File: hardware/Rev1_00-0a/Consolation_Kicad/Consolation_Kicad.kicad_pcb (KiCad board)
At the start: 2 copper layers, 137.5 x 76.6 mm, 392 parts, among them J10 61300311121, J11 5051102291, J12 RPI_CMx_B, J13 5051102291, J14 61300311121, J15 61300311121, J17 61300311121, J18 61300411121, J19 RPI_CMx_A, J2 SJ-3524-SMT-TR, J3 62684-402100ALF, J4 12401598E4#2A, J5 S2B-PH-K-S, J6 2086581001, J7 2998TR, J8 DM3AT-SF-PEJM5, Q1 SSM3K56FS,LF, Q10 SSM3K56FS,LF, Q11 SSM3K56FS,LF, Q14 SSM3K56FS,LF, Q18 SSM3K56FS,LF, Q19 SSM3K56FS,LF, Q2 SSM3K56FS,LF, Q20 SSM3K56FS,LF, Q21 SSM3K56FS,LF, Q22 SSM3K56FS,LF, Q23 SSM3K56FS,LF, Q24 SSM3K56FS,LF, Q25 SSM3K56FS,LF, Q26 SSM3K56FS,LF, Q27 SSM3K56FS,LF, Q28 SSM3K56FS,LF, Q3 SSM3K56FS,LF, Q7 SSM3K56FS,LF, Q8 SSM3K56FS,LF, Q9 SSM3K56FS,LF, U1 BQ25640VDLR, U10 TPS62826DMQR, U11 AP22913W6-7, U15 SN65DSI84ZXHR, U18 AP22913W6-7, U19 SN74LVC1G125DBVR, U2 RP2350A, U21 MCP7940NT-I/MS, U26 TPS61169DCKR, U30 STM6710DWB6F, U31 SN74LVC1G125DBVR, U32 SN74HCS365QPWRQ1, U4 ECS-2016MVQ-120-BP-TR, U5 NAU88C22YG, U6 AP22913W6-7, U7 TPS79901DRVR, U8 GD25Q32CWIGR, U9 TPS61230ARNSR, Y1 12MHz 10pF, Y2 32.768kHz

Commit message: Component preliminary placement
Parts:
- removed R136: 22R, footprint:RES_0402
- added R212: 10K, footprint:RES_0402, F.Cu at (151.1, 155.3)
- moved C123 420.3 mm to (35.9, 25.2)
- moved R121 420.3 mm to (24.6, 24.6)
- moved R124 420.3 mm to (24.6, 26.6)
- moved R176 420.3 mm to (24.6, 28.8)
- moved R180 420.3 mm to (24.6, 30.9)
- moved R40 420.3 mm to (24.6, 20.4)
- moved R41 420.3 mm to (24.6, 22.4)
- moved C122 420.3 mm to (35.9, 23.1)
- moved D13 420.3 mm to (36.2, 18.4)
- moved D14 420.3 mm to (36.2, 20.8)
- moved D19 420.3 mm to (20.2, 34.6)
- moved Q14 420.3 mm to (37.1, 30.6)
- moved HOLE7 377.0 mm to (58.9, 53.4)
- moved J5 368.3 mm to (51.9, 109.4), turned to -90 degrees
- moved HOLE6 364.5 mm to (58.9, 123.4)
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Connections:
- J19 pad 24: /CM5_CONN_A/GPIO19 -> /CM5_CONN_A/GPIO26
- J19 pad 45: /CM5_CONN_A/GPIO24 -> unconnected-(J19-GPIO24-Pad45)
- R171 pad 1: /CM5_CONN_A/GPIO19 -> /CM5_CONN_A/GPIO26
- R209 pad 2: /~{TFT_RST} -> /TFT CONN/TFT_3V3
- R211 pad 2: /TFT_PWR_EN -> /~{TFT_RST}
- R271 pad 2: 3V3 -> 5V0
- U11 pad 3: /TFT_PWR_EN -> /~{TFT_RST}
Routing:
- added copper zone on In1.Cu, net GND
- added copper zone on In4.Cu, net GND
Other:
- copper layers 2 -> 6

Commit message: Preliminary placement of Consolation continues
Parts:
- removed C115, C116: 0.1u, footprint:CAP_NONPOL_0402
- removed D44, D45: D1213A-02SOL-7, footprint:SOT-23-3
- removed R13, R14, R15, R16, R17: 10K, footprint:RES_ARRAY_4_1206
- added D1: ESD7351HT1G, footprint:SOD-323, F.Cu at (76.0, 52.4)
- added D20: ESD7351HT1G, footprint:SOD-323, F.Cu at (56.2, 147.5)
- added D23: ESD7351HT1G, footprint:SOD-323, F.Cu at (56.2, 150.3)
- added D24: ESD7351HT1G, footprint:SOD-323, F.Cu at (56.2, 153.0)
- added D25: ESD7351HT1G, footprint:SOD-323, F.Cu at (56.2, 155.8)
- added D26: ESD7016MUTAG, footprint:UDFN8, F.Cu at (108.8, 114.5)
- added R181: 10K, footprint:RES_0402, F.Cu at (66.1, 59.6)
- added R185: 10K, footprint:RES_0402, F.Cu at (66.1, 61.7)
- added R186: 10K, footprint:RES_0402, F.Cu at (66.1, 63.8)
- added R187: 10K, footprint:RES_0402, F.Cu at (66.1, 65.9)
- added R188: 10K, footprint:RES_0402, F.Cu at (66.1, 68.0)
- added R189: 10K, footprint:RES_0402, F.Cu at (69.1, 59.6)
- added R190: 10K, footprint:RES_0402, F.Cu at (69.1, 61.7)
- added R191: 10K, footprint:RES_0402, F.Cu at (69.1, 63.8)
- added R192: 10K, footprint:RES_0402, F.Cu at (69.1, 65.9)
- added R193: 10K, footprint:RES_0402, F.Cu at (69.1, 68.0)
- added R194: 10K, footprint:RES_0402, F.Cu at (72.1, 59.6)
- added R195: 10K, footprint:RES_0402, F.Cu at (72.1, 61.7)
- added R196: 10K, footprint:RES_0402, F.Cu at (72.1, 63.8)
- added R197: 10K, footprint:RES_0402, F.Cu at (72.1, 65.9)
- added R198: 10K, footprint:RES_0402, F.Cu at (72.1, 68.0)
- added R199: 10K, footprint:RES_0402, F.Cu at (75.1, 59.6)
- added R200: 10K, footprint:RES_0402, F.Cu at (75.1, 61.7)
- added R201: 10K, footprint:RES_0402, F.Cu at (75.1, 63.8)
- added R202: 10K, footprint:RES_0402, F.Cu at (75.1, 65.9)
- added R203: 10K, footprint:RES_0402, F.Cu at (75.1, 68.0)
- D19: value D1213A-02SOL-7 -> ESD7351HT1G; footprint footprint:SOT-23-3 -> footprint:SOD-323
- moved D19 122.8 mm to (141.7, 52.4), turned to -90 degrees
- moved R121 118.7 mm to (140.2, 51.7), turned to 90 degrees
- moved R120 64.3 mm to (106.5, 83.0)
- moved R141 63.1 mm to (131.6, 81.1), turned to 180 degrees
- moved R140 61.8 mm to (131.6, 77.7)
- moved R171 60.8 mm to (131.6, 82.2), turned to 180 degrees
- moved R127 60.2 mm to (131.6, 78.8), turned to 180 degrees
- moved R144 59.9 mm to (131.6, 80.0), turned to 180 degrees
- moved R115 59.9 mm to (140.4, 81.5)
- moved R125 59.3 mm to (140.4, 74.5)
- moved R124 58.6 mm to (77.6, 51.7), turned to 90 degrees
- moved R117 58.0 mm to (140.4, 83.8)
- moved R161 57.3 mm to (131.6, 76.5), turned to 180 degrees
- moved R116 56.6 mm to (140.4, 80.3), turned to 180 degrees
- moved R83 55.6 mm to (131.6, 74.5), turned to 180 degrees
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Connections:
- C122 pad 2: Net-(C122-Pad2) -> Net-(D19-K)
- D19 pad 1: /CM5_CONN_A/~{VOL_UP} -> Net-(D19-K)
- D19 pad 2: /CM5_CONN_A/~{VOL_DOWN} -> GND
- D5 pad 1: /CONTROLLER/L_THUMBST_SW -> /CONTROLLER/L_THUMBST_X
- D5 pad 2: /CONTROLLER/L_DPAD_UP -> /CONTROLLER/L_THUMBST_Y
- D5 pad 4: /CONTROLLER/L_DPAD_DOWN -> /CONTROLLER/L_THUMBST_SW
- D5 pad 5: /CONTROLLER/L_DPAD_LEFT -> /CONTROLLER/L_DPAD_UP
- D5 pad 7: /CONTROLLER/L_DPAD_RIGHT -> /CONTROLLER/L_DPAD_DOWN
- D5 pad 8: /CONTROLLER/L_START -> unconnected-(D5-I/O6-Pad8)
- D6 pad 1: /CONTROLLER/R_THUMBST_SW -> /CONTROLLER/R_THUMBST_X
- D6 pad 2: /CONTROLLER/R_BTN_A -> /CONTROLLER/R_THUMBST_Y
- D6 pad 4: /CONTROLLER/R_BTN_B -> /CONTROLLER/R_THUMBST_SW
- D6 pad 5: /CONTROLLER/R_BTN_X -> /CONTROLLER/R_BTN_A
- D6 pad 7: /CONTROLLER/R_BTN_Y -> /CONTROLLER/R_BTN_B
- D6 pad 8: /CONTROLLER/R_SELECT -> unconnected-(D6-I/O6-Pad8)
- D8 pad 1: /CONTROLLER/L_L1_TRIG -> /CONTROLLER/L_DPAD_LEFT
- D8 pad 2: /CONTROLLER/L_L2_TRIG -> /CONTROLLER/L_DPAD_RIGHT
- D8 pad 4: /CONTROLLER/L_HOME -> /CONTROLLER/L_START
- D8 pad 5: unconnected-(D8-I/O4-Pad5) -> /CONTROLLER/L_L1_TRIG
- D8 pad 7: unconnected-(D8-I/O5-Pad7) -> /CONTROLLER/L_L2_TRIG
- D8 pad 8: unconnected-(D8-I/O6-Pad8) -> /CONTROLLER/L_HOME
- D9 pad 1: /CONTROLLER/R_L1_TRIG -> /CONTROLLER/R_BTN_X
- D9 pad 2: /CONTROLLER/R_L2_TRIG -> /CONTROLLER/R_BTN_Y
- D9 pad 4: /CONTROLLER/R_EXTRA -> /CONTROLLER/R_SELECT
- D9 pad 5: unconnected-(D9-I/O4-Pad5) -> /CONTROLLER/R_L1_TRIG
- D9 pad 7: unconnected-(D9-I/O5-Pad7) -> /CONTROLLER/R_L2_TRIG
- D9 pad 8: unconnected-(D9-I/O6-Pad8) -> /CONTROLLER/R_EXTRA
- R121 pad 2: Net-(C122-Pad2) -> Net-(D19-K)
- R127 pad 1: /CM5_CONN_A/I2C3.I2C_SCL -> /I2C2.I2C_SCL
- R176 pad 1: Net-(C122-Pad2) -> Net-(D19-K)
- R83 pad 1: /CM5_CONN_A/I2C3.I2C_SDA -> /I2C2.I2C_SDA
- S2 pad 2: Net-(C122-Pad2) -> Net-(D19-K)
- U21 pad 5: /CM5_CONN_A/I2C3.I2C_SDA -> /I2C2.I2C_SDA
- U21 pad 6: /CM5_CONN_A/I2C3.I2C_SCL -> /I2C2.I2C_SCL
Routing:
- net /CM5_CONN_A/GPIO12: track 0.00 -> 2.66 mm
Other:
- board text added: "Controller - L"
- board text added: "Controller - R"

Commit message: Work on preliminary placement + RP2350A fanout
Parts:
- removed C128, C130: 1u, footprint:CAP_NONPOL_0805
- removed C129, C131, C151: 0.1u, footprint:CAP_NONPOL_0402
- removed C13, C14: 10u, footprint:CAP_NONPOL_1210
- removed R11: 0R, footprint:RES_0603
- removed R160: 10K, footprint:RES_0402
- removed R4: 0R, footprint:RES_1206
- added C45: 4.7u, footprint:CAP_NONPOL_0805, F.Cu at (87.0, 58.6)
- added C46: 4.7u, footprint:CAP_NONPOL_0805, F.Cu at (87.0, 56.6)
- added R13: 0R, footprint:RES_1206, F.Cu at (43.1, 86.6)
- added R14: 0R, footprint:RES_1206, F.Cu at (20.8, 105.0)
- added R204: 0R, footprint:RES_0402, F.Cu at (84.7, 71.6)
- moved R182 168.1 mm to (22.6, 123.0)
- moved R168 167.9 mm to (25.1, 124.4)
- moved R43 166.7 mm to (27.6, 123.9)
- moved C155 75.8 mm to (144.3, 85.7), turned to 90 degrees
- moved C16 54.0 mm to (85.5, 73.3), turned to 180 degrees
- moved D11 53.1 mm to (21.7, 66.2)
- moved S1 52.1 mm to (55.1, 59.1), turned to -90 degrees
- moved C17 51.2 mm to (83.3, 73.3)
- moved C140 51.1 mm to (90.0, 71.7), turned to 90 degrees
- moved R280 51.0 mm to (87.8, 73.9), turned to 90 degrees
- moved C120 50.1 mm to (17.3, 69.6)
- moved C147 48.3 mm to (91.7, 72.2), turned to 90 degrees
- moved C134 47.3 mm to (91.0, 64.8), turned to 180 degrees
- moved R37 45.8 mm to (43.8, 71.6), turned to -90 degrees
- moved C27 45.8 mm to (44.7, 74.4)
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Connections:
- net /CM5_CONN_B/RP2350_USB_VBUS renamed /CM5_CONN_B/RP2350_VBUS
- net Net-(U2B-USB_DN) renamed /CONTROLLER/USB_N
- net Net-(U2B-USB_DP) renamed /CONTROLLER/USB_P
- C103 pad 2: /Power Supply/VSYS -> Net-(U10-VIN)
- C23 pad 2: /Power Supply/VSYS -> Net-(L3-+)
- C24 pad 2: /Power Supply/VSYS -> Net-(L3-+)
- C29 pad 2: /Power Supply/VSYS -> Net-(L3-+)
- C30 pad 2: /Power Supply/VSYS -> Net-(U10-VIN)
- C31 pad 2: /Power Supply/VSYS -> Net-(U10-VIN)
- C32 pad 2: /Power Supply/VSYS -> Net-(U10-VIN)
- C6 pad 2: Net-(L1--) -> /Power Supply/VSYS
- C7 pad 2: Net-(L1--) -> /Power Supply/VSYS
- C91 pad 2: Net-(L1--) -> /Power Supply/VSYS
- C98 pad 2: /Power Supply/VSYS -> Net-(L3-+)
- D26 pad 1: unconnected-(D26-I/O1-Pad1) -> Net-(D26-I/O1)
- D26 pad 7: Net-(D26-I/O5) -> unconnected-(D26-I/O5-Pad7)
- J4 pad A5: Net-(D26-I/O5) -> Net-(D26-I/O1)
- L1 pad 2: Net-(L1--) -> /Power Supply/VSYS
- L3 pad 1: /Power Supply/VSYS -> Net-(L3-+)
- R10 pad 1: /CONTROLLER/CM5_USB3_1.USB_N -> /CM5_CONN_B/USB2_RP2350.USB_N
- R157 pad 1: /CONTROLLER/L_THUMBST_SW -> /CONTROLLER/L_DPAD_LEFT
- R159 pad 1: /CONTROLLER/R_THUMBST_SW -> /CONTROLLER/L_DPAD_RIGHT
- R181 pad 1: /CONTROLLER/L_HOME -> /CONTROLLER/R_THUMBST_X
- R185 pad 1: /CONTROLLER/R_EXTRA -> /CONTROLLER/R_THUMBST_Y
- R186 pad 1: /CONTROLLER/R_BTN_Y -> /CONTROLLER/L_DPAD_DOWN
- R187 pad 1: /CONTROLLER/R_BTN_X -> /CONTROLLER/L_DPAD_UP
- R188 pad 1: /CONTROLLER/R_BTN_B -> /CONTROLLER/L_THUMBST_SW
- R189 pad 1: /CONTROLLER/R_BTN_A -> /CONTROLLER/L_THUMBST_Y
- R190 pad 1: /CONTROLLER/L_START -> /CONTROLLER/R_EXTRA
- R191 pad 1: /CONTROLLER/R_SELECT -> /CONTROLLER/L_THUMBST_X
- R192 pad 1: /CONTROLLER/L_THUMBST_X -> /CONTROLLER/L_START
- R193 pad 1: /CONTROLLER/L_THUMBST_Y -> /CONTROLLER/L_L1_TRIG
- R194 pad 1: /CONTROLLER/R_THUMBST_X -> /CONTROLLER/L_L2_TRIG
- R195 pad 1: /CONTROLLER/R_THUMBST_Y -> /CONTROLLER/L_HOME
- R196 pad 1: /CONTROLLER/L_DPAD_RIGHT -> /CONTROLLER/R_L2_TRIG
- R197 pad 1: /CONTROLLER/L_DPAD_LEFT -> /CONTROLLER/R_L1_TRIG
- R198 pad 1: /CONTROLLER/L_DPAD_DOWN -> /CONTROLLER/R_SELECT
- R199 pad 1: /CONTROLLER/L_DPAD_UP -> /CONTROLLER/R_BTN_Y
- R200 pad 1: /CONTROLLER/R_L2_TRIG -> /CONTROLLER/R_BTN_X
- R201 pad 1: /CONTROLLER/R_L1_TRIG -> /CONTROLLER/R_BTN_B
- R202 pad 1: /CONTROLLER/L_L2_TRIG -> /CONTROLLER/R_BTN_A
- R203 pad 1: /CONTROLLER/L_L1_TRIG -> /CONTROLLER/R_THUMBST_SW
- R37 pad 2: /Power Supply/VSYS -> Net-(L3-+)
- R9 pad 1: /CONTROLLER/CM5_USB3_1.USB_P -> /CM5_CONN_B/USB2_RP2350.USB_P
- U1 pad 1: Net-(D26-I/O5) -> Net-(D26-I/O1)
- U1 pad 13: Net-(L1--) -> /Power Supply/VSYS
- U10 pad 6: /Power Supply/VSYS -> Net-(U10-VIN)
- U2 pad 10: /CONTROLLER/R_EXTRA -> /CONTROLLER/R_THUMBST_Y
- U2 pad 12: /CONTROLLER/L_L1_TRIG -> /CONTROLLER/R_THUMBST_SW
- U2 pad 13: /CONTROLLER/L_L2_TRIG -> /CONTROLLER/R_BTN_A
- U2 pad 14: /CONTROLLER/R_L1_TRIG -> /CONTROLLER/R_BTN_B
- U2 pad 15: /CONTROLLER/R_L2_TRIG -> /CONTROLLER/R_BTN_X
- U2 pad 16: /CONTROLLER/L_DPAD_UP -> /CONTROLLER/R_BTN_Y
- U2 pad 17: /CONTROLLER/L_DPAD_DOWN -> /CONTROLLER/R_SELECT
- U2 pad 18: /CONTROLLER/L_DPAD_LEFT -> /CONTROLLER/R_L1_TRIG
- U2 pad 19: /CONTROLLER/L_DPAD_RIGHT -> /CONTROLLER/R_L2_TRIG
- U2 pad 27: /CONTROLLER/L_START -> /CONTROLLER/R_EXTRA
- U2 pad 28: /CONTROLLER/R_SELECT -> /CONTROLLER/L_THUMBST_X
- U2 pad 31: /CONTROLLER/R_BTN_A -> /CONTROLLER/L_THUMBST_Y
- U2 pad 32: /CONTROLLER/R_BTN_B -> /CONTROLLER/L_THUMBST_SW
- U2 pad 33: /CONTROLLER/R_BTN_X -> /CONTROLLER/L_DPAD_UP
- U2 pad 34: /CONTROLLER/R_BTN_Y -> /CONTROLLER/L_DPAD_DOWN
- U2 pad 35: /CONTROLLER/L_THUMBST_SW -> /CONTROLLER/L_DPAD_LEFT
- U2 pad 37: /CONTROLLER/R_THUMBST_SW -> /CONTROLLER/L_DPAD_RIGHT
- U2 pad 40: /CONTROLLER/L_THUMBST_X -> /CONTROLLER/L_START
- U2 pad 41: /CONTROLLER/L_THUMBST_Y -> /CONTROLLER/L_L1_TRIG
- U2 pad 42: /CONTROLLER/R_THUMBST_X -> /CONTROLLER/L_L2_TRIG
- U2 pad 43: /CONTROLLER/R_THUMBST_Y -> /CONTROLLER/L_HOME
- U2 pad 9: /CONTROLLER/L_HOME -> /CONTROLLER/R_THUMBST_X
- U9 pad 2: /Power Supply/VSYS -> Net-(L3-+)
- U9 pad 4: /Power Supply/VSYS -> Net-(L3-+)
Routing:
- net GND: track 0.00 -> 37.1 mm, vias 0 -> 45
- net 3V3: track 0.00 -> 27.0 mm, vias 0 -> 10
- net /CONTROLLER/1V1_CORE: track 0.00 -> 18.4 mm, vias 0 -> 5
- net /CONTROLLER/R_BTN_Y: track 0.00 -> 11.0 mm
- net /CONTROLLER/R_SELECT: track 0.00 -> 10.7 mm
- net /CONTROLLER/R_L1_TRIG: track 0.00 -> 10.2 mm
- net /CONTROLLER/L_THUMBST_X: track 0.00 -> 9.75 mm
- net /CONTROLLER/L_THUMBST_Y: track 0.00 -> 9.73 mm
- net /CONTROLLER/R_L2_TRIG: track 0.00 -> 9.71 mm
- net /CONTROLLER/R_BTN_X: track 0.00 -> 9.41 mm
- net /CONTROLLER/R_THUMBST_Y: track 0.00 -> 9.26 mm
- net /CONTROLLER/L_THUMBST_SW: track 0.00 -> 9.12 mm
- net /CONTROLLER/L_DPAD_RIGHT: track 0.00 -> 9.11 mm
- net /CONTROLLER/R_EXTRA: track 0.00 -> 8.99 mm
- net /CONTROLLER/R_BTN_B: track 0.00 -> 8.91 mm
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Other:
- outline, holes or cut-outs redrawn
- board text added: "~{RP2350 USB BOOT}"

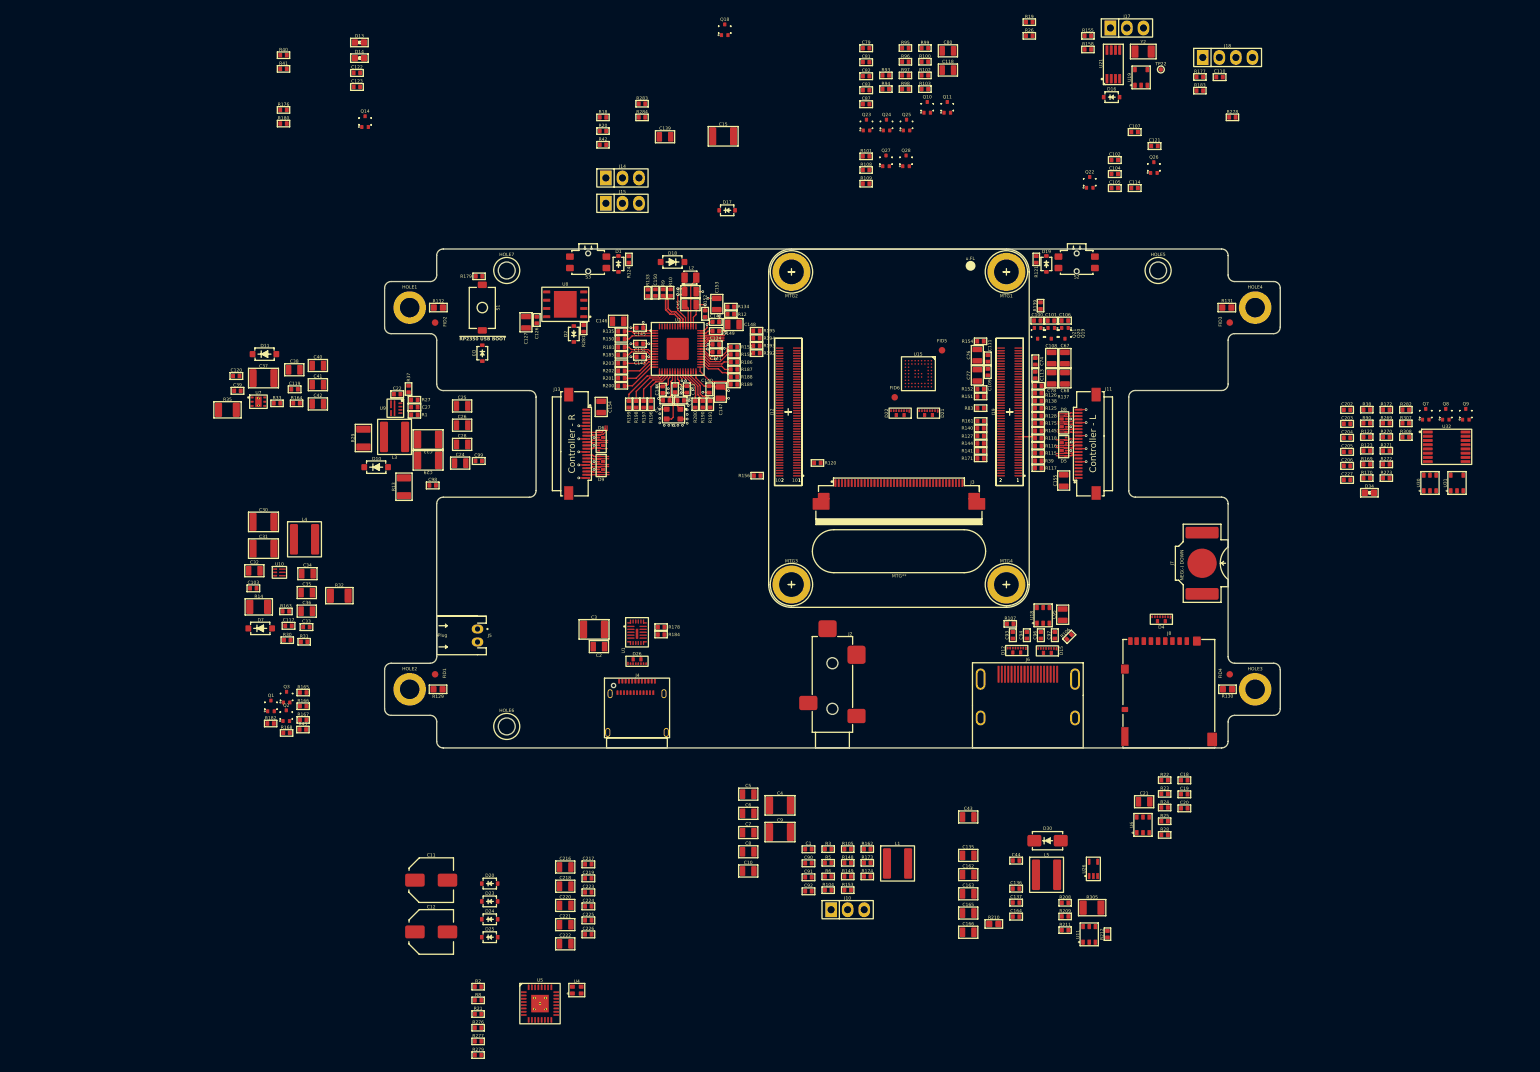
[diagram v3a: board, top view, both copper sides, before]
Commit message: Update ConJoy L2 trigger (2-level trigger instead) Update ConJoy all output files accordingly
Work on Consolation preliminary placement
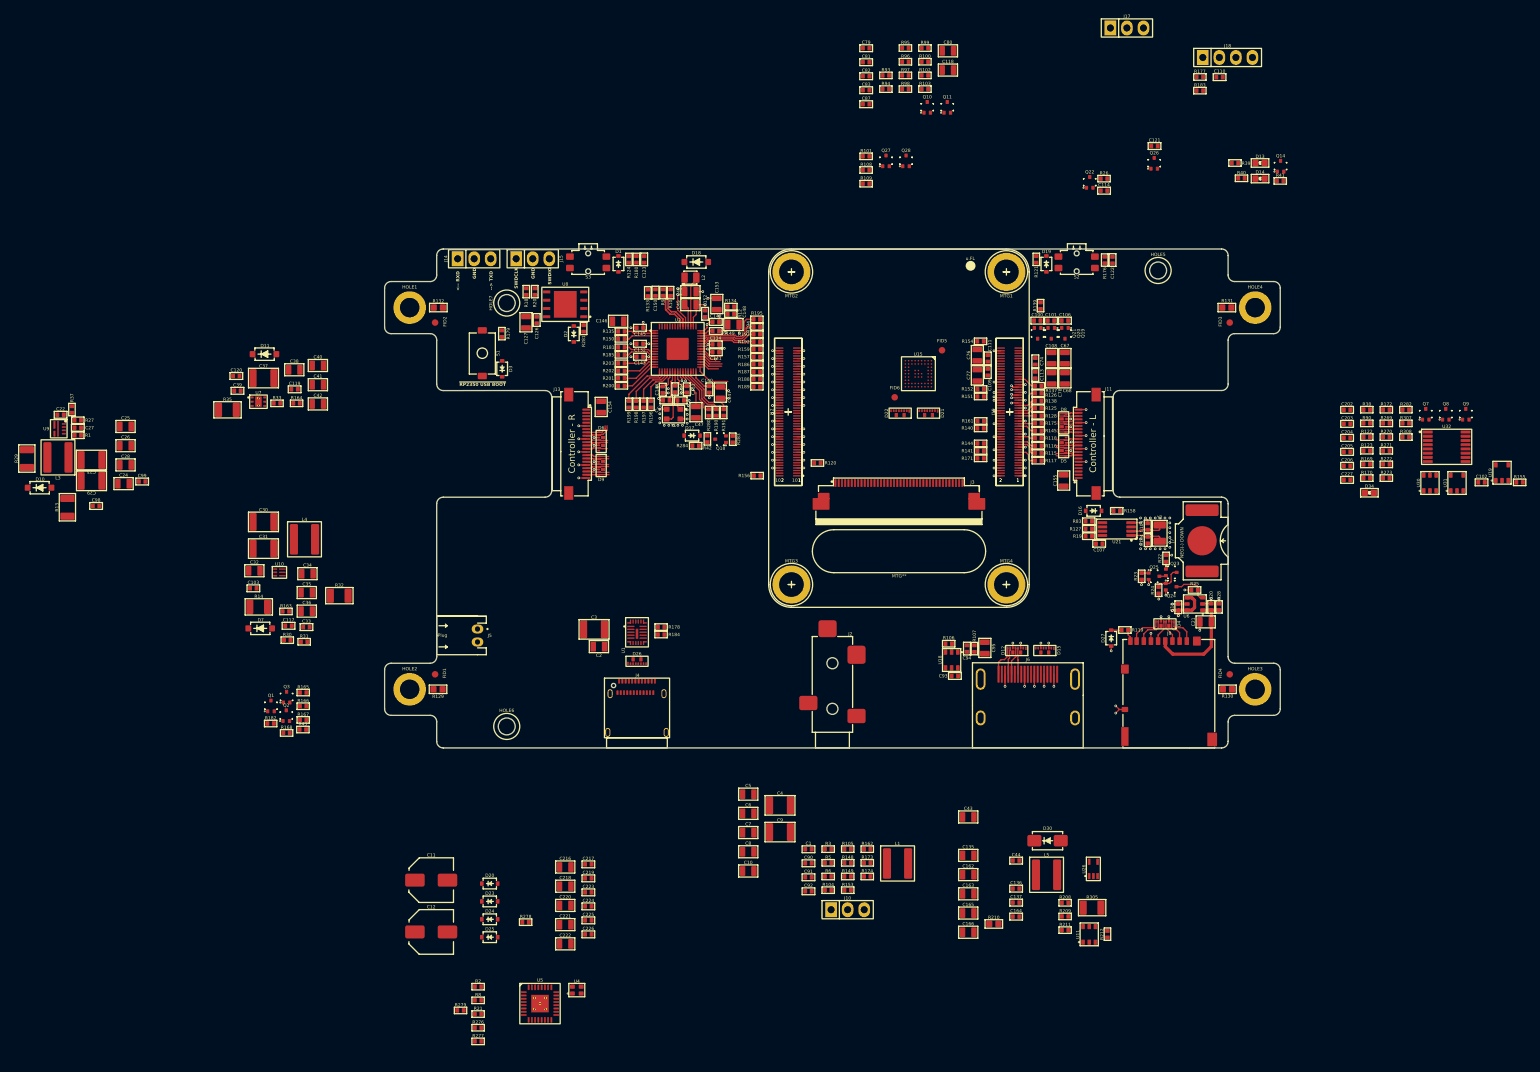
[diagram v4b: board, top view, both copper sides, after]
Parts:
- removed C139: 1u, footprint:CAP_NONPOL_0805
- removed C15: 10u, footprint:CAP_NONPOL_1210
- removed C19, C96, C97: 0.1u, footprint:CAP_NONPOL_0402
- removed TP22: 28 mils, footprint:SMT_TP_28_MILS
- added C47: 4.7u, footprint:CAP_NONPOL_0805, F.Cu at (87.9, 75.2)
- added D27: ESD7351HT1G, footprint:SOD-323, F.Cu at (151.7, 109.8)
- added R119: 22R, footprint:RES_0402, F.Cu at (153.7, 108.6)
- moved R278 164.4 mm to (61.8, 153.4)
- moved R41 154.0 mm to (177.6, 39.6)
- moved R40 148.3 mm to (171.7, 39.2)
- moved Q14 140.7 mm to (177.7, 37.4)
- moved D13 139.5 mm to (174.5, 36.9)
- moved D14 139.5 mm to (174.5, 39.3)
- moved R176 128.2 mm to (150.7, 51.8), turned to -90 degrees
- moved C122 119.5 mm to (151.8, 51.8), turned to 90 degrees
- moved R155 95.4 mm to (214.4, 85.9)
- moved Q24 83.3 mm to (160.8, 102.0), turned to -90 degrees
- moved Q23 83.1 mm to (160.9, 99.8), turned to -90 degrees
- moved U19 82.2 mm to (211.7, 84.5)
- moved R19 79.5 mm to (148.2, 94.2), turned to 180 degrees
- moved Q25 79.0 mm to (158.2, 100.3), turned to -90 degrees
- moved C102 75.0 mm to (208.5, 85.9)
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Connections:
- D12 pad 3: /HDMI/5V_HDMI0 -> GND
- D15 pad 3: /HDMI/5V_HDMI0 -> GND
- D4 pad 3: /SD_CARD/SD_VDD -> GND
- J8 pad 9: /SD_CARD/SD_CARD_DETECT -> Net-(J8-CD_B)
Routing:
- net GND: track 37.1 -> 120.3 mm, vias 45 -> 139
- net /SD_CARD/SD_VDD: track 0.00 -> 17.0 mm
- net 3V3: track 27.0 -> 38.9 mm, vias 10 -> 17
- net /CONTROLLER/L_HOME: track 6.96 -> 13.7 mm
- net /CM5_CONN_A/SDIO_D1: track 0.00 -> 6.37 mm, vias 0 -> 1
- net /CONTROLLER/L_L2_TRIG: track 6.92 -> 12.9 mm
- net /CM5_CONN_A/SDIO_D0: track 0.00 -> 5.80 mm, vias 0 -> 1
- net Net-(Q24-D): track 0.00 -> 5.78 mm
- net /CM5_CONN_A/SDIO_D2: track 0.00 -> 5.58 mm, vias 0 -> 1
- net Net-(U21-X2): track 0.00 -> 5.27 mm
- net Net-(U21-X1): track 0.00 -> 5.22 mm
- net /CONTROLLER/L_L1_TRIG: track 7.15 -> 12.2 mm
- net /CM5_CONN_A/SDIO_D3: track 0.00 -> 4.88 mm, vias 0 -> 1
- net /CM5_CONN_B/HDMI0.HPD: track 0.00 -> 4.88 mm
- net /CONTROLLER/L_START: track 7.18 -> 11.9 mm
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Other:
- outline, holes or cut-outs redrawn
- board text added: "--> TXD"
- board text added: "<-- RXD"
- board text added: "GND"
- board text added: "SWDCLK"
- board text added: "SWDIO"
